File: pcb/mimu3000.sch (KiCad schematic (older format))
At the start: 13 parts, among them SW1 ONOFF, U1 AQY211EH, U2 ATTINY48U

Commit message: Capacitance needed?
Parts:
- added C?: 0.1uF, Capacitor_SMD:C_2512_6332Metric, symbol Device:C
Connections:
- net +3V0: now also C?.1
- net GND: now also C?.2
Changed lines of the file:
@@
 Wire Wire Line
 	4950 3400 5900 3400
+$Comp
+L Device:C C?
+U 1 1 5E3D87F9
+P 5300 6050
+F 0 "C?" H 5415 6096 50  0000 L CNN
+F 1 "0.1uF" H 5415 6005 50  0000 L CNN
+F 2 "Capacitor_SMD:C_2512_6332Metric" H 5338 5900 50  0001 C CNN
+F 3 "~" H 5300 6050 50  0001 C CNN
+	1    5300 6050
+	1    0    0    -1
+$EndComp
+Wire Wire Line
+	5300 5900 5300 5800
+Connection ~ 5300 5800
+$Comp
+L power:GND #PWR?
+U 1 1 5E3DA51E
+P 5300 6200
+F 0 "#PWR?" H 5300 5950 50  0001 C CNN
+F 1 "GND" H 5305 6027 50  0000 C CNN
+F 2 "" H 5300 6200 50  0001 C CNN
+F 3 "" H 5300 6200 50  0001 C CNN
+	1    5300 6200
+	1    0    0    -1
+$EndComp
 $EndSCHEMATC

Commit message: We have to use Attiny88
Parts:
- C2: renamed from C?; footprint Capacitor_SMD:C_2512_6332Metric -> Capacitor_SMD:C_0805_2012Metric_Pad1.15x1.40mm_HandSolder
- U2: value ATTINY48U -> ATTINY88AU; footprint Housings_QFP:TQFP-32_7x7mm_Pitch0.8mm -> Package_DFN_QFN:QFN-32-1EP_5x5mm_P0.5mm_EP3.1x3.1mm
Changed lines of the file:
@@
 P 7350 5800
 F 0 "U2" V 7300 6300 50  0000 C CNN
-F 1 "ATTINY48U" H 7350 5800 50  0000 C CNN
-F 2 "Housings_QFP:TQFP-32_7x7mm_Pitch0.8mm" H 7950 5800 50  0001 C CIN
-F 3 "" H 6550 6150 50  0001 C CNN
+F 1 "ATTINY88AU" H 7350 5800 50  0000 C CNN
+F 2 "Package_DFN_QFN:QFN-32-1EP_5x5mm_P0.5mm_EP3.1x3.1mm" H 7950 5800 50  0001 C CIN
+F 3 "../doc/ATtiny4888" H 6550 6150 50  0001 C CNN
 	1    7350 5800
 	0    -1   -1   0
@@
 	4950 3400 5900 3400
 $Comp
-L Device:C C?
+L Device:C C2
 U 1 1 5E3D87F9
 P 5300 6050
-F 0 "C?" H 5415 6096 50  0000 L CNN
+F 0 "C2" H 5415 6096 50  0000 L CNN
 F 1 "0.1uF" H 5415 6005 50  0000 L CNN
-F 2 "Capacitor_SMD:C_2512_6332Metric" H 5338 5900 50  0001 C CNN
+F 2 "Capacitor_SMD:C_0805_2012Metric_Pad1.15x1.40mm_HandSolder" H 5338 5900 50  0001 C CNN
 F 3 "~" H 5300 6050 50  0001 C CNN
 	1    5300 6050
@@
 Connection ~ 5300 5800
 $Comp
-L power:GND #PWR?
+L power:GND #PWR0101
 U 1 1 5E3DA51E
 P 5300 6200
-F 0 "#PWR?" H 5300 5950 50  0001 C CNN
+F 0 "#PWR0101" H 5300 5950 50  0001 C CNN
 F 1 "GND" H 5305 6027 50  0000 C CNN
 F 2 "" H 5300 6200 50  0001 C CNN

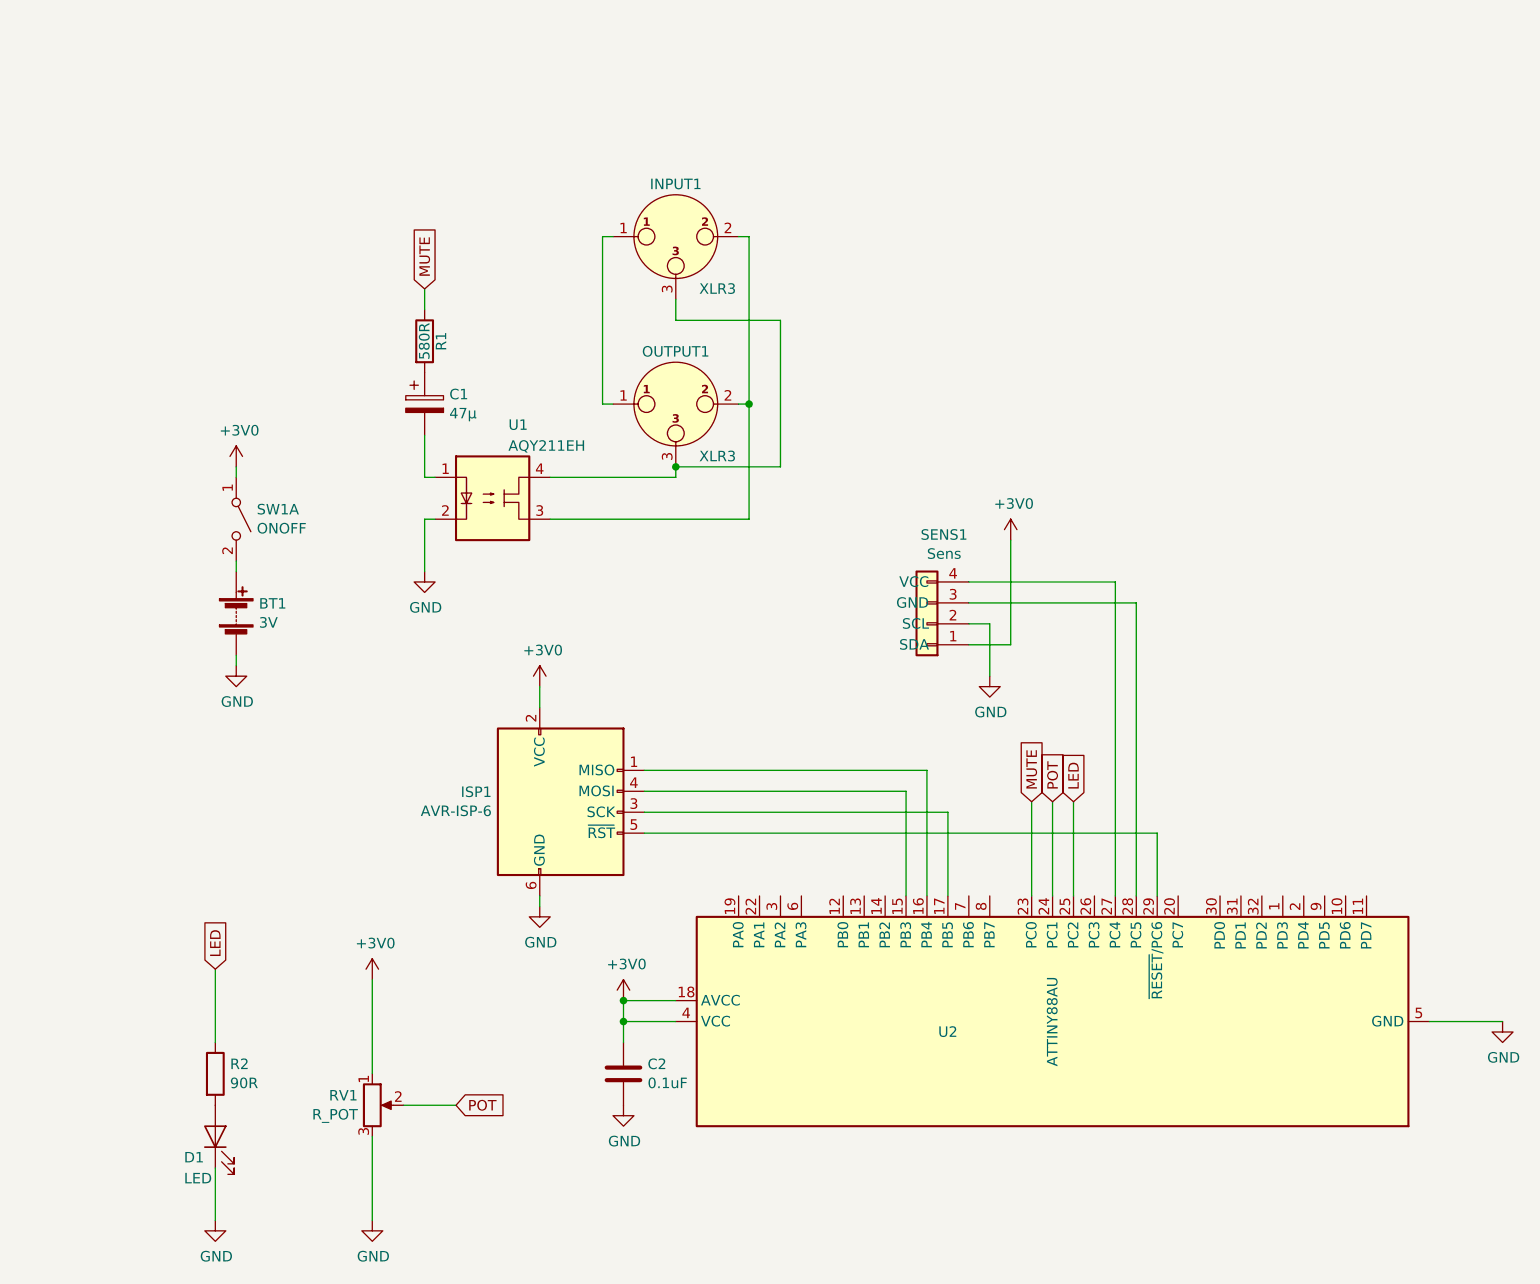
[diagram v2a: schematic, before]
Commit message: Added 3 extra IO
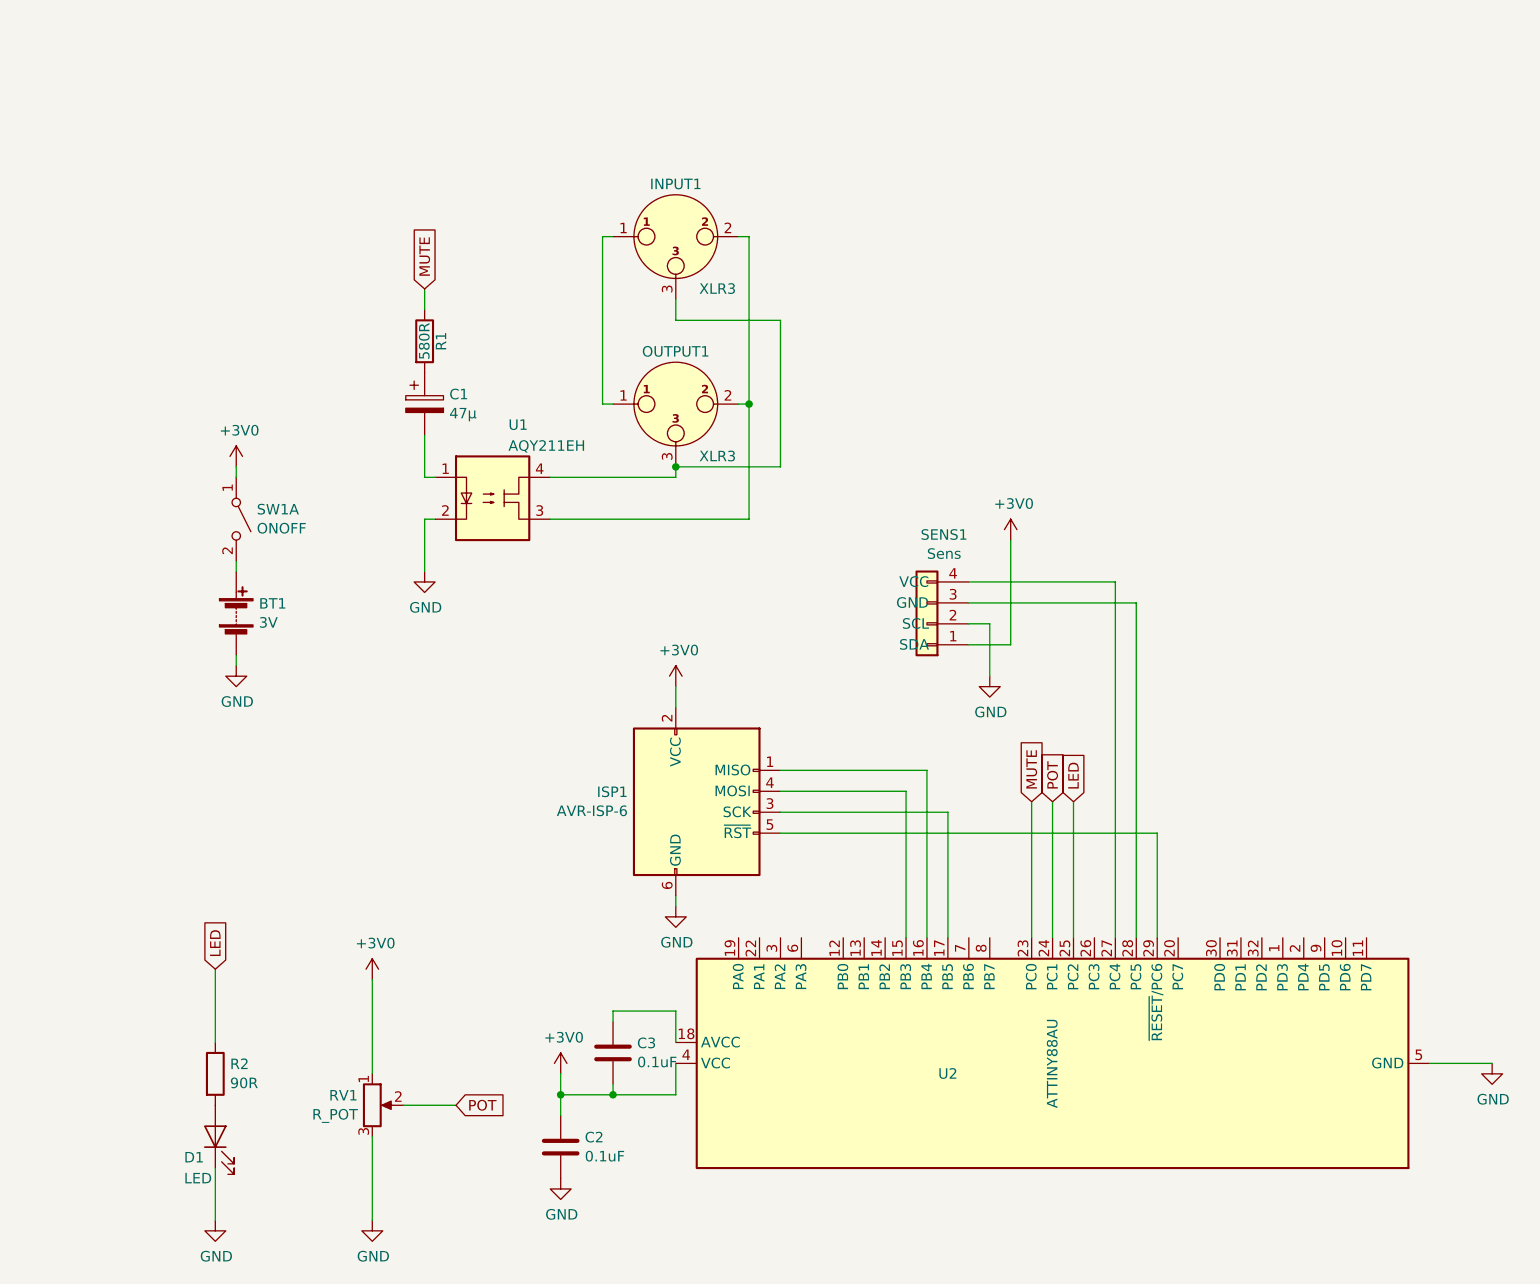
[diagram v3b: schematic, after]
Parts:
- added C3: 0.1uF, Capacitor_SMD:C_0805_2012Metric_Pad1.15x1.40mm_HandSolder, symbol Device:C
- U2: footprint Package_DFN_QFN:QFN-32-1EP_5x5mm_P0.5mm_EP3.1x3.1mm -> Package_QFP:TQFP-32_7x7mm_P0.8mm
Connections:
- net +3V0: now also C3.2; no longer U2.18 (AVCC)
- new net: C3.1, U2.18 (AVCC)
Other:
- moved on the sheet: C2, ISP1, U2
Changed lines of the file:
@@
 L MCU_Microchip_ATtiny:ATtiny48-AU U2
 U 1 1 5E29D77C
-P 7350 5800
-F 0 "U2" V 7300 6300 50  0000 C CNN
-F 1 "ATTINY88AU" H 7350 5800 50  0000 C CNN
-F 2 "Package_DFN_QFN:QFN-32-1EP_5x5mm_P0.5mm_EP3.1x3.1mm" H 7950 5800 50  0001 C CIN
-F 3 "../doc/ATtiny4888" H 6550 6150 50  0001 C CNN
-	1    7350 5800
+P 7350 6000
+F 0 "U2" V 7300 6500 50  0000 C CNN
+F 1 "ATTINY88AU" H 7350 6000 50  0000 C CNN
+F 2 "Package_QFP:TQFP-32_7x7mm_P0.8mm" H 7950 6000 50  0001 C CIN
+F 3 "../doc/ATtiny4888" H 6550 6350 50  0001 C CNN
+	1    7350 6000
 	0    -1   -1   0
 $EndComp
@@
 L Connector:AVR-ISP-6 ISP1
 U 1 1 5E2B28C5
-P 5000 4800
-F 0 "ISP1" H 4671 4896 50  0000 R CNN
-F 1 "AVR-ISP-6" H 4671 4805 50  0000 R CNN
-F 2 "Connector_PinHeader_2.54mm:PinHeader_2x03_P2.54mm_Vertical" V 4750 4850 50  0001 C CNN
-F 3 " ~" H 3725 4250 50  0001 C CNN
-	1    5000 4800
-	1    0    0    -1
-$EndComp
-Wire Wire Line
-	4900 5250 4900 5200
-Wire Wire Line
-	4900 4300 4900 4200
+P 5650 4800
+F 0 "ISP1" H 5321 4896 50  0000 R CNN
+F 1 "AVR-ISP-6" H 5321 4805 50  0000 R CNN
+F 2 "Connector_PinHeader_2.54mm:PinHeader_2x03_P2.54mm_Vertical" V 5400 4850 50  0001 C CNN
+F 3 " ~" H 4375 4250 50  0001 C CNN
+	1    5650 4800
+	1    0    0    -1
+$EndComp
+Wire Wire Line
+	5550 5250 5550 5200
+Wire Wire Line
+	5550 4300 5550 4200
 Wire Wire Line
 	4100 6050 4100 5600
 Wire Wire Line
-	9150 5800 9500 5800
-Wire Wire Line
-	5550 5800 5300 5800
-Wire Wire Line
-	5300 5700 5300 5800
-Wire Wire Line
-	5300 5700 5550 5700
-Wire Wire Line
-	7850 4900 7850 5200
-Wire Wire Line
-	6650 5200 6650 4700
-Wire Wire Line
-	6750 5200 6750 4600
-Wire Wire Line
-	6850 5200 6850 4800
-Wire Wire Line
-	7650 5200 7650 3700
+	9150 6000 9450 6000
+Wire Wire Line
+	7850 4900 7850 5400
+Wire Wire Line
+	6650 5400 6650 4700
+Wire Wire Line
+	6750 5400 6750 4600
+Wire Wire Line
+	6850 5400 6850 4800
+Wire Wire Line
+	7650 5400 7650 3700
 Wire Wire Line
 	6950 3700 7650 3700
 Wire Wire Line
-	7750 3800 7750 5200
+	7750 3800 7750 5400
 Wire Wire Line
 	6950 3800 7750 3800
@@
 L power:+3V0 #PWR05
 U 1 1 5E4210BA
-P 4900 4200
-F 0 "#PWR05" H 4900 4050 50  0001 C CNN
-F 1 "+3V0" H 4915 4373 50  0000 C CNN
-F 2 "" H 4900 4200 50  0001 C CNN
-F 3 "" H 4900 4200 50  0001 C CNN
-	1    4900 4200
+P 5550 4200
+F 0 "#PWR05" H 5550 4050 50  0001 C CNN
+F 1 "+3V0" H 5565 4373 50  0000 C CNN
+F 2 "" H 5550 4200 50  0001 C CNN
+F 3 "" H 5550 4200 50  0001 C CNN
+	1    5550 4200
 	1    0    0    -1
 $EndComp
@@
 L power:+3V0 #PWR09
 U 1 1 5E4218B0
-P 5300 5700
-F 0 "#PWR09" H 5300 5550 50  0001 C CNN
-F 1 "+3V0" H 5315 5873 50  0000 C CNN
-F 2 "" H 5300 5700 50  0001 C CNN
-F 3 "" H 5300 5700 50  0001 C CNN
-	1    5300 5700
-	1    0    0    -1
-$EndComp
-Connection ~ 5300 5700
+P 5000 6050
+F 0 "#PWR09" H 5000 5900 50  0001 C CNN
+F 1 "+3V0" H 5015 6223 50  0000 C CNN
+F 2 "" H 5000 6050 50  0001 C CNN
+F 3 "" H 5000 6050 50  0001 C CNN
+	1    5000 6050
+	1    0    0    -1
+$EndComp
 $Comp
 L power:+3V0 #PWR08
@@
 L power:GND #PWR07
 U 1 1 5E423825
-P 4900 5250
-F 0 "#PWR07" H 4900 5000 50  0001 C CNN
-F 1 "GND" H 4905 5077 50  0000 C CNN
-F 2 "" H 4900 5250 50  0001 C CNN
-F 3 "" H 4900 5250 50  0001 C CNN
-	1    4900 5250
-	1    0    0    -1
-$EndComp
-Wire Wire Line
-	5400 4900 7850 4900
-Wire Wire Line
-	5400 4800 6850 4800
-Wire Wire Line
-	5400 4700 6650 4700
-Wire Wire Line
-	5400 4600 6750 4600
+P 5550 5250
+F 0 "#PWR07" H 5550 5000 50  0001 C CNN
+F 1 "GND" H 5555 5077 50  0000 C CNN
+F 2 "" H 5550 5250 50  0001 C CNN
+F 3 "" H 5550 5250 50  0001 C CNN
+	1    5550 5250
+	1    0    0    -1
+$EndComp
+Wire Wire Line
+	6050 4900 7850 4900
+Wire Wire Line
+	6050 4800 6850 4800
+Wire Wire Line
+	6050 4700 6650 4700
+Wire Wire Line
+	6050 4600 6750 4600
 $Comp
 L power:GND #PWR010
 U 1 1 5E4346AD
-P 9500 5800
-F 0 "#PWR010" H 9500 5550 50  0001 C CNN
-F 1 "GND" H 9505 5627 50  0000 C CNN
-F 2 "" H 9500 5800 50  0001 C CNN
-F 3 "" H 9500 5800 50  0001 C CNN
-	1    9500 5800
+P 9450 6000
+F 0 "#PWR010" H 9450 5750 50  0001 C CNN
+F 1 "GND" H 9455 5827 50  0000 C CNN
+F 2 "" H 9450 6000 50  0001 C CNN
+F 3 "" H 9450 6000 50  0001 C CNN
+	1    9450 6000
 	1    0    0    -1
 $EndComp
@@
 LED
 Wire Wire Line
-	7450 5200 7450 4750
+	7450 5400 7450 4750
 Wire Wire Line
 	4100 6350 4100 6750
@@
 POT
 Wire Wire Line
-	7350 5200 7350 4750
+	7350 5400 7350 4750
 Text GLabel 4350 2300 1    50   Input ~ 0
 MUTE
@@
 MUTE
 Wire Wire Line
-	7250 4750 7250 5200
+	7250 4750 7250 5400
 Wire Wire Line
 	4400 3400 4350 3400
@@
 L Device:C C2
 U 1 1 5E3D87F9
-P 5300 6050
-F 0 "C2" H 5415 6096 50  0000 L CNN
-F 1 "0.1uF" H 5415 6005 50  0000 L CNN
-F 2 "Capacitor_SMD:C_0805_2012Metric_Pad1.15x1.40mm_HandSolder" H 5338 5900 50  0001 C CNN
-F 3 "~" H 5300 6050 50  0001 C CNN
-	1    5300 6050
-	1    0    0    -1
-$EndComp
-Wire Wire Line
-	5300 5900 5300 5800
-Connection ~ 5300 5800
+P 5000 6400
+F 0 "C2" H 5115 6446 50  0000 L CNN
+F 1 "0.1uF" H 5115 6355 50  0000 L CNN
+F 2 "Capacitor_SMD:C_0805_2012Metric_Pad1.15x1.40mm_HandSolder" H 5038 6250 50  0001 C CNN
+F 3 "~" H 5000 6400 50  0001 C CNN
+	1    5000 6400
+	1    0    0    -1
+$EndComp
 $Comp
 L power:GND #PWR0101
 U 1 1 5E3DA51E
-P 5300 6200
-F 0 "#PWR0101" H 5300 5950 50  0001 C CNN
-F 1 "GND" H 5305 6027 50  0000 C CNN
-F 2 "" H 5300 6200 50  0001 C CNN
-F 3 "" H 5300 6200 50  0001 C CNN
-	1    5300 6200
-	1    0    0    -1
-$EndComp
+P 5000 6550
+F 0 "#PWR0101" H 5000 6300 50  0001 C CNN
+F 1 "GND" H 5005 6377 50  0000 C CNN
+F 2 "" H 5000 6550 50  0001 C CNN
+F 3 "" H 5000 6550 50  0001 C CNN
+	1    5000 6550
+	1    0    0    -1
+$EndComp
+$Comp
+L Device:C C3
+U 1 1 5E3E8912
+P 5250 5950
+F 0 "C3" H 5365 5996 50  0000 L CNN
+F 1 "0.1uF" H 5365 5905 50  0000 L CNN
+F 2 "Capacitor_SMD:C_0805_2012Metric_Pad1.15x1.40mm_HandSolder" H 5288 5800 50  0001 C CNN
+F 3 "~" H 5250 5950 50  0001 C CNN
+	1    5250 5950
+	1    0    0    -1
+$EndComp
+Wire Wire Line
+	5000 6250 5000 6150
+Wire Wire Line
+	5000 6150 5250 6150
+Wire Wire Line
+	5550 6150 5550 6000
+Connection ~ 5000 6150
+Wire Wire Line
+	5000 6050 5000 6150
+Wire Wire Line
+	5250 6150 5250 6100
+Connection ~ 5250 6150
+Wire Wire Line
+	5250 6150 5550 6150
+Wire Wire Line
+	5250 5800 5250 5750
+Wire Wire Line
+	5250 5750 5550 5750
+Wire Wire Line
+	5550 5900 5550 5750
 $EndSCHEMATC

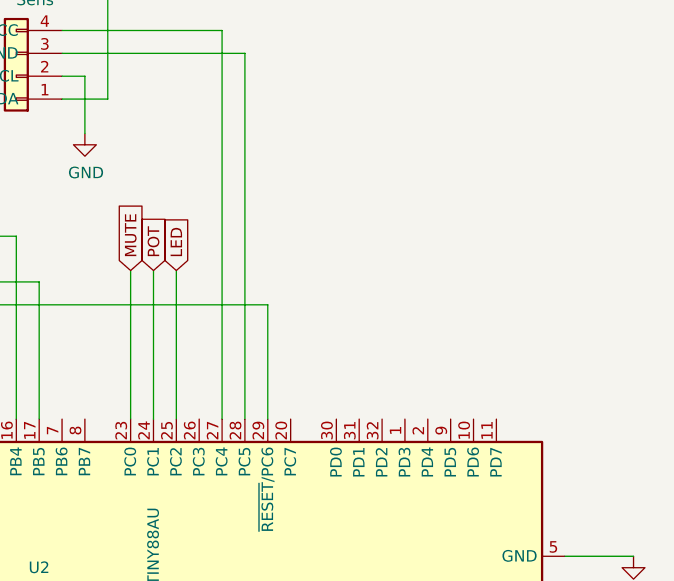
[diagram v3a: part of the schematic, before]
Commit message: Use realworld-potentiometer
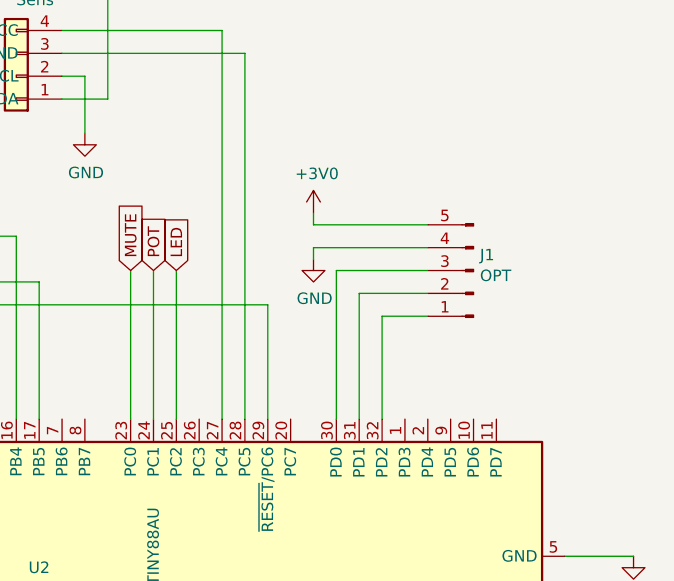
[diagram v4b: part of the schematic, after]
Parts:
- added J1: OPT, Connector_PinHeader_1.27mm:PinHeader_1x05_P1.27mm_Vertical, symbol Connector:Conn_01x05_Male
- SENS1: footprint Connector_PinHeader_2.54mm:PinHeader_1x04_P2.54mm_Vertical -> Connector_JST:JST_EH_B4B-EH-A_1x04_P2.50mm_Vertical
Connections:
- net +3V0: now also J1.5 (Pin_5)
- net GND: now also J1.4 (Pin_4)
- net at U2.30 (PD0): now also J1.3 (Pin_3)
- net at U2.31 (PD1): now also J1.2 (Pin_2)
- net at U2.32 (PD2): now also J1.1 (Pin_1)
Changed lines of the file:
@@
 F 0 "SENS1" H 6668 3475 50  0000 C CNN
 F 1 "Sens" H 6668 3566 50  0000 C CNN
-F 2 "Connector_PinHeader_2.54mm:PinHeader_1x04_P2.54mm_Vertical" H 6750 3900 50  0001 C CNN
+F 2 "Connector_JST:JST_EH_B4B-EH-A_1x04_P2.50mm_Vertical" H 6750 3900 50  0001 C CNN
 F 3 "~" H 6750 3900 50  0001 C CNN
 	1    6750 3900
@@
 Wire Wire Line
 	5550 5900 5550 5750
+$Comp
+L Connector:Conn_01x05_Male J1
+U 1 1 5E3F474D
+P 8750 4750
+F 0 "J1" H 8722 4682 50  0000 R CNN
+F 1 "OPT" H 8722 4773 50  0000 R CNN
+F 2 "Connector_PinHeader_1.27mm:PinHeader_1x05_P1.27mm_Vertical" H 8750 4750 50  0001 C CNN
+F 3 "~" H 8750 4750 50  0001 C CNN
+	1    8750 4750
+	-1   0    0    1
+$EndComp
+Wire Wire Line
+	8350 5400 8350 4950
+$Comp
+L power:GND #PWR0102
+U 1 1 5E3FB13A
+P 8050 4700
+F 0 "#PWR0102" H 8050 4450 50  0001 C CNN
+F 1 "GND" H 8055 4527 50  0000 C CNN
+F 2 "" H 8050 4700 50  0001 C CNN
+F 3 "" H 8050 4700 50  0001 C CNN
+	1    8050 4700
+	1    0    0    -1
+$EndComp
+Wire Wire Line
+	8350 4950 8550 4950
+Wire Wire Line
+	8250 4850 8550 4850
+Wire Wire Line
+	8250 4850 8250 5400
+Wire Wire Line
+	8150 4750 8550 4750
+Wire Wire Line
+	8150 4750 8150 5400
+$Comp
+L power:+3V0 #PWR0103
+U 1 1 5E40BA3B
+P 8050 4500
+F 0 "#PWR0103" H 8050 4350 50  0001 C CNN
+F 1 "+3V0" H 8065 4673 50  0000 C CNN
+F 2 "" H 8050 4500 50  0001 C CNN
+F 3 "" H 8050 4500 50  0001 C CNN
+	1    8050 4500
+	1    0    0    -1
+$EndComp
+Wire Wire Line
+	8550 4650 8050 4650
+Wire Wire Line
+	8050 4650 8050 4700
+Wire Wire Line
+	8550 4550 8050 4550
+Wire Wire Line
+	8050 4550 8050 4500
 $EndSCHEMATC

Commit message: something
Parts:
- BT1: value 3V -> 4.5V
- R1: value 580R -> 110R
- R2: value 90R -> 165R
- RV1: value R_POT -> 1K_POT; footprint Potentiometer_THT:Potentiometer_Alps_RK09Y11_Single_Horizontal -> custom:Potentiometer_Generic_5mm_Single_Horizontal
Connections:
- net +3V0: now also RV1.3; no longer RV1.1
- net GND: now also RV1.1; no longer RV1.3
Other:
- moved on the sheet: BT1, C1, C2, C3, D1, INPUT1, ISP1, J1, OUTPUT1, R1, R2, RV1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
